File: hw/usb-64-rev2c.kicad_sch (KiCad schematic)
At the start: 11 parts, among them J1 USB_C_Receptacle_PowerOnly_6P, U100 NCP1117-3.3_SOT223

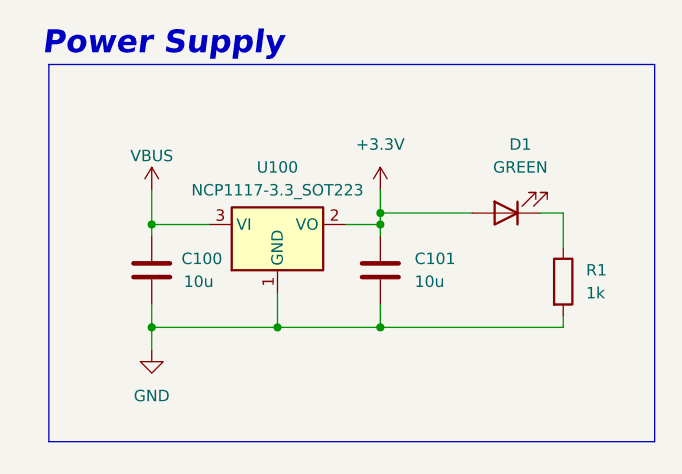
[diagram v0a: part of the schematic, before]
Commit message: changed pcb specs
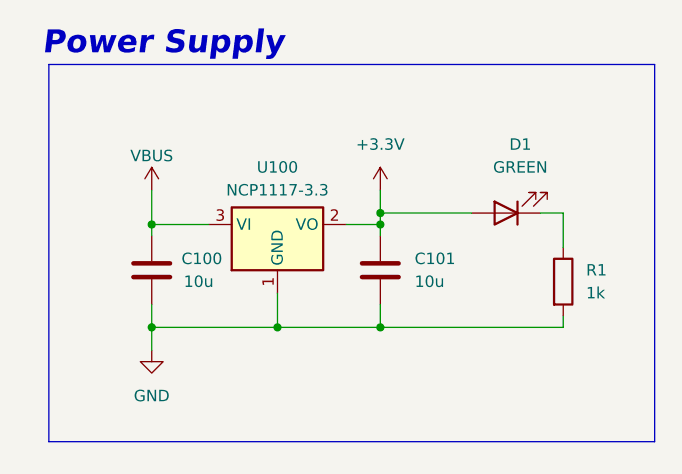
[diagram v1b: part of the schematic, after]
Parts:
- U100: value NCP1117-3.3_SOT223 -> NCP1117-3.3
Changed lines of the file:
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@@
 			)
 		)
-		(property "Value" "NCP1117-3.3_SOT223"
+		(property "Value" "NCP1117-3.3"
 			(at 43.18 34.29 0)
 			(effects

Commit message: rerouted
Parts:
- C5, C6: footprint Capacitor_SMD:C_0402_1005Metric -> Capacitor_SMD:C_0603_1608Metric
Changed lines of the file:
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@@
 			)
 		)
-		(property "Footprint" "Capacitor_SMD:C_0402_1005Metric"
+		(property "Footprint" "Capacitor_SMD:C_0603_1608Metric"
 			(at 98.7552 105.41 0)
 			(effects
@@
 			)
 		)
-		(property "Footprint" "Capacitor_SMD:C_0402_1005Metric"
+		(property "Footprint" "Capacitor_SMD:C_0603_1608Metric"
 			(at 74.6252 105.41 0)
 			(effects

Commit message: 1p version
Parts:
- removed C100, C101: 10u, Capacitor_SMD:C_0805_2012Metric, symbol Device:C
- removed D1: GREEN, LED_SMD:LED_0805_2012Metric, symbol Device:LED
- removed R1: 1k, Resistor_SMD:R_0402_1005Metric, symbol Device:R
- removed U100: NCP1117-3.3, Package_TO_SOT_SMD:SOT-223-3_TabPin2, symbol Regulator_Linear:NCP1117-3.3_SOT223
- added C3, C4: 4.7u, Capacitor_SMD:C_1206_3216Metric, symbol Device:C
- added D1: ESD7L5.0DT5G, Package_TO_SOT_SMD:SOT-723, symbol Power_Protection:ESDA5V3L
- added D2: D_Schottky, Diode_SMD:D_SOD-323, symbol Device:D_Schottky
- added D6, D7: RED, LED_SMD:LED_0603_1608Metric, symbol Device:LED
- added IC1: NCP708MU330TAG, Package_SON:SON95P300X300X55-7N, symbol NCP708MU330TAG:NCP708MU330TAG
- added J2: USB_A, Connector_USB:CONN_UJ2-AH-SMT_CUD, symbol Connector:USB_A
- added R6, R9: 330, Resistor_SMD:R_0402_1005Metric, symbol Device:R
- renumbered C5 to C1, C6 to C2
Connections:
- net +3.3V: now also C4.1, D6.2 (A), IC1.4 (OUT), IC1.5 (OUT_S)
- net GND: now also C3.2, C4.2, D1.3 (A), IC1.2 (GND), IC1.7 (EN_2), J2.4 (GND), R6.2, R9.2
- net VBUS: now also C3.1, D2.2 (A), IC1.1 (EN_1), IC1.6 (IN); no longer C1.1, FB3.1, J1.A9 (VBUS), J1.B9 (VBUS)
- new net: D2.1 (K), J2.1 (VBUS)
- new net: D7.1 (K), R9.1
- new net: D6.1 (K), R6.1
- new net: C1.1, FB3.1, J1.A9 (VBUS), J1.B9 (VBUS)
- new net MCU/GPIO25: D7.2 (A)
- new net USB_MCU_D_N: D1.2 (K), J2.2 (D-)
- new net USB_MCU_D_P: D1.1 (K), J2.3 (D+)
- no-connect marks 1 -> 2
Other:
- removed sheet USB
- removed sheet misc
- sheet C64_controls ports: added IO_DOWN, IO_FIRE, IO_LEFT, IO_RIGHT, IO_UP; removed none
- sheet MCU ports: added +3.3V, GPIO25, IO_DOWN, IO_FIRE, IO_LEFT, IO_RIGHT, IO_UP, USB_MCU_D_N, USB_MCU_D_P; removed none
- note removed: "Power Supply"
- moved on the sheet: C1, C2, FB3, J1, R7, R8

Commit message: pre production review
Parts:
- removed D1: ESD7L5.0DT5G, Package_TO_SOT_SMD:SOT-723, symbol Power_Protection:ESDA5V3L
- removed IC1: NCP708MU330TAG, Package_SON:SON95P300X300X55-7N, symbol NCP708MU330TAG:NCP708MU330TAG
- added H1: MountingHole, MountingHole:MountingHole_2.2mm_M2, symbol Mechanical:MountingHole
- added U1: TPD2EUSB30, Package_TO_SOT_SMD:Texas_DRT-3, symbol Power_Protection:TPD2EUSB30
- added U2: TLV76733DRVx, Package_SON:WSON-6-1EP_2x2mm_P0.65mm_EP1x1.6mm_ThermalVias, symbol Regulator_Linear:TLV76733DRVx
- C1: value 1u -> 10n; footprint Capacitor_SMD:C_0603_1608Metric -> Capacitor_SMD:C_0402_1005Metric; LCSC Part # (none) -> C15195
- C2: value 1u -> 100n; LCSC Part # (none) -> C14663
- C3: value 4.7u -> 1u; footprint Capacitor_SMD:C_1206_3216Metric -> Capacitor_SMD:C_0603_1608Metric; LCSC Part # C29823 -> C15849
- C4: value 4.7u -> 10u; footprint Capacitor_SMD:C_1206_3216Metric -> Capacitor_SMD:C_0805_2012Metric; LCSC Part # C29823 -> C440198
- R6, R9: value 330 -> 1k; LCSC Part # C25104 -> C11702
- renumbered FB3 to FB1
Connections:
- net +3.3V: now also U2.1 (OUT), U2.2 (SNS)
- net GND: now also U1.3 (GND), U2.3 (GND), U2.5 (GND), U2.7 (PAD)
- net USB_MCU_D_N: now also U1.2 (D-)
- net USB_MCU_D_P: now also U1.1 (D+)
- net VBUS: now also C1.1, FB1.1, J1.A9 (VBUS), J1.B9 (VBUS); no longer C2.1, C3.1, FB1.2
- new net +5V: C2.1, C3.1, FB1.2, U2.4 (EN), U2.6 (IN)
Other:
- note added: "C4 X5R (effective capacitance at least 0.5uF)"
- note added: "Device connector"
- note added: "High level view"
- note added: "PMIC"
- note added: "Unfiltered VBUS for peripherals"
- note added: "VBUS filter"
- note added: "X7R"
- moved on the sheet: C3, C4, D2, D6, D7, FB1, J1, J2, R6, R7, R8, R9
